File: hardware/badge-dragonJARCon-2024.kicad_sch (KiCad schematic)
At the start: 32 parts, among them J1 UART, J2 Battery, J3 OLED, J5 Shitty addon, P1 USB_C_Plug_USB2.0, Q1 DMG3415U-7, SW1 ON, SW2 RESET, SW3 BOOT, SW4 PB4, SW5 PB3, SW6 PB1, SW7 PB2, U1 ESP32-C6-WROOM-1U-N4, U2 AP2112K-3.3

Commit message: feat(Hw): Init floorplan
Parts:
- removed C9: 0.1uF, Capacitor_SMD:C_0603_1608Metric, symbol Device:C
- removed D3: WS2812B, Ekoparty:LED_SK6812MINI_PLCC4_3.5x3.5mm_P1.75mm, symbol LED:WS2812B
- removed R6: 470, Resistor_SMD:R_0603_1608Metric, symbol Device:R
- removed U1: ESP32-C6-WROOM-1U-N4, Footprint:MOD28_ESP32-C6-WROOM-1U_EXP, symbol Minino:ESP32-C6-WROOM-1U-N8
- added C10, C11: 10uF, Capacitor_SMD:C_0603_1608Metric, symbol Device:C_Small
- added C9: 1uF, Capacitor_SMD:C_0603_1608Metric, symbol Device:C_Small
- added D2: LED_RABG, Footprints:AAA3528SURKCGKC09, symbol Device:LED_RABG
- added R5, R7, R8: 330, Resistor_SMD:R_0603_1608Metric, symbol Device:R
- added U1: ESP32-C6-WROOM-1-N4, Footprints:ESP32C6WROOM1N4, symbol ESP32-C6-WROOM-1-N4:ESP32-C6-WROOM-1-N4
- J2: footprint Footprint:BAT-TH_BH-AAA-A1AJ024 -> Footprints:BAT-TH_BH-AAA-A1AJ024
- J3: footprint Connector_PinHeader_2.54mm:PinHeader_1x04_P2.54mm_Vertical -> Footprints:Display OLED 128 x32
- J5: footprint (none) -> Connector_PinHeader_2.54mm:PinHeader_2x02_P2.54mm_Vertical
- P1: footprint Footprint:C393939 -> Footprints:C393939
- SW1: footprint Footprint:JS102011SAQN -> Footprints:JS102011SAQN
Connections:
- net +3V3: now also C10.1, C11.1, C9.1, D2.2 (A), U1.2 (3V3)
- net BOOT: now also U1.15 (IO9)
- net D+: now also U1.14 (IO13)
- net D-: now also U1.13 (IO12)
- net EN: now also U1.3 (EN)
- net GND: now also C10.2, C11.2, C9.2, U1.1 (GND_1), U1.28 (GND_2), U1.29 (GND_3), U1.30 (GND_4), U1.31 (GND_5), U1.32 (GND_6), U1.33 (GND_7), U1.34 (GND_8), U1.35 (GND_9), U1.36 (GND_10), U1.37 (GND_11)
- net RX: now also U1.24 (RXD0)
- net SCL: now also U1.7 (IO7)
- net SDA: now also U1.6 (IO6)
- net TX: now also U1.25 (TXD0)
- new net: D2.1 (RK), R5.2
- new net: D2.3 (BK), R8.2
- new net: D2.4 (GK), R7.2
- new net BACK: U1.20 (IO22)
- new net BLUE: R8.1, U1.12 (IO11)
- new net DOWN: U1.21 (IO23)
- new net GREEN: R7.1, U1.26 (IO3)
- new net RED: R5.1, U1.27 (IO2)
- new net SELECT: U1.9 (IO1)
- new net UP: U1.23 (IO15)
- no-connect marks 13 -> 9
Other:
- note added: "MICROCONTROLLER"
- note removed: "ESP32-C6"
- moved on the sheet: F1, P1, R2, R3

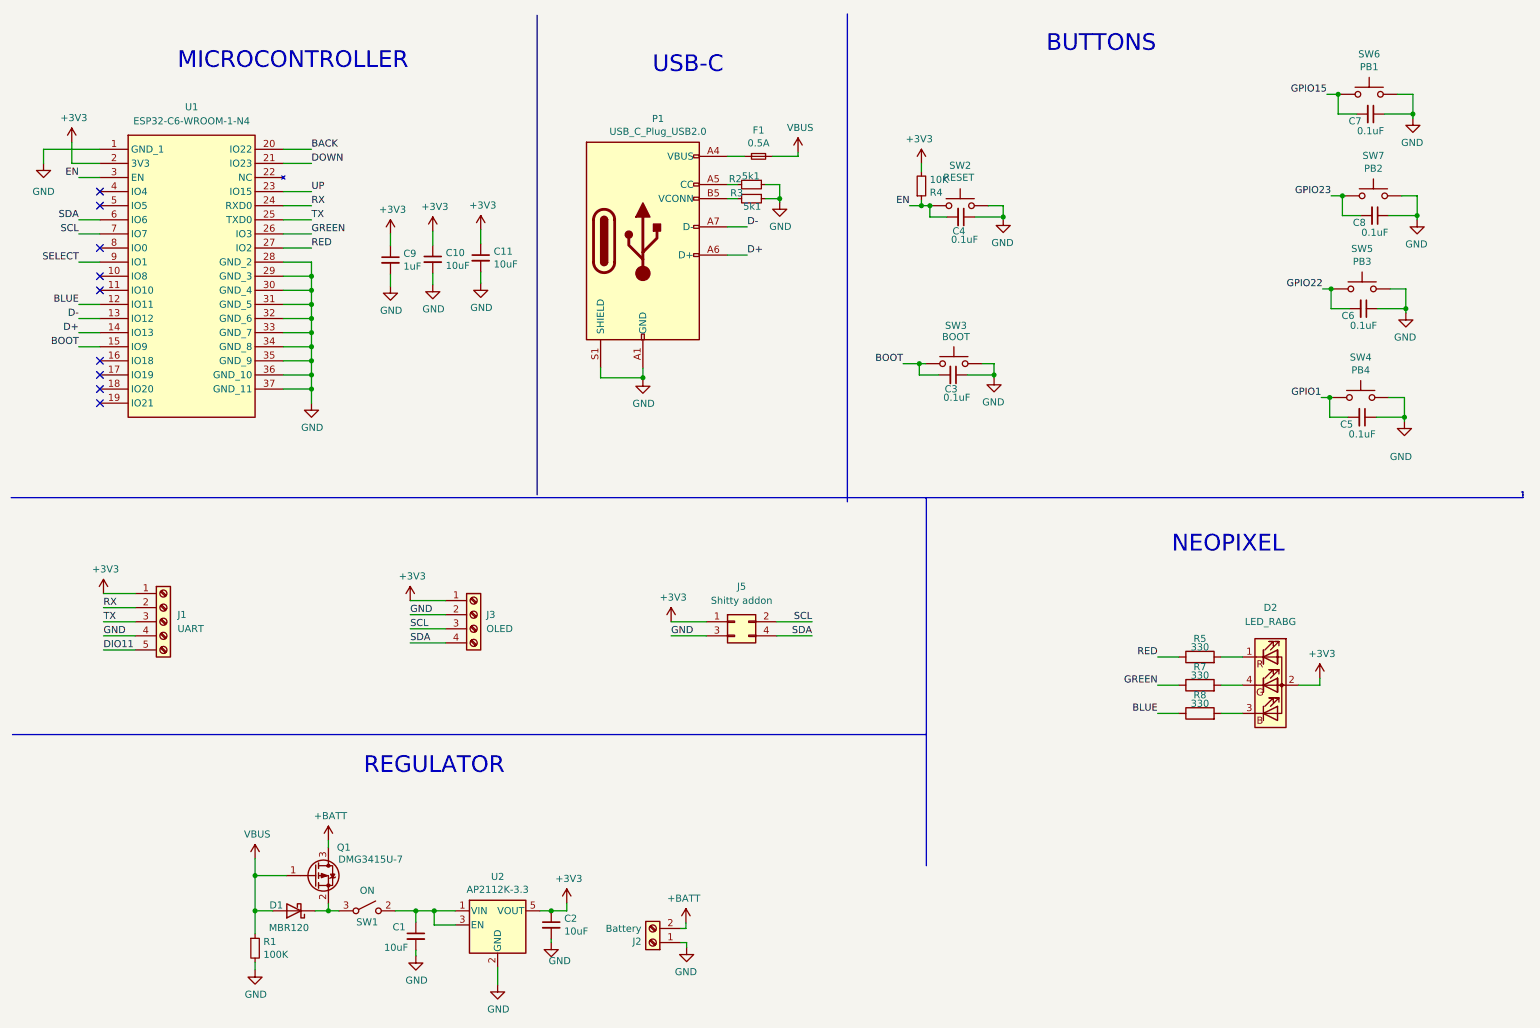
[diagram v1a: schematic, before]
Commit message: feat(Hw): Start new floorplan
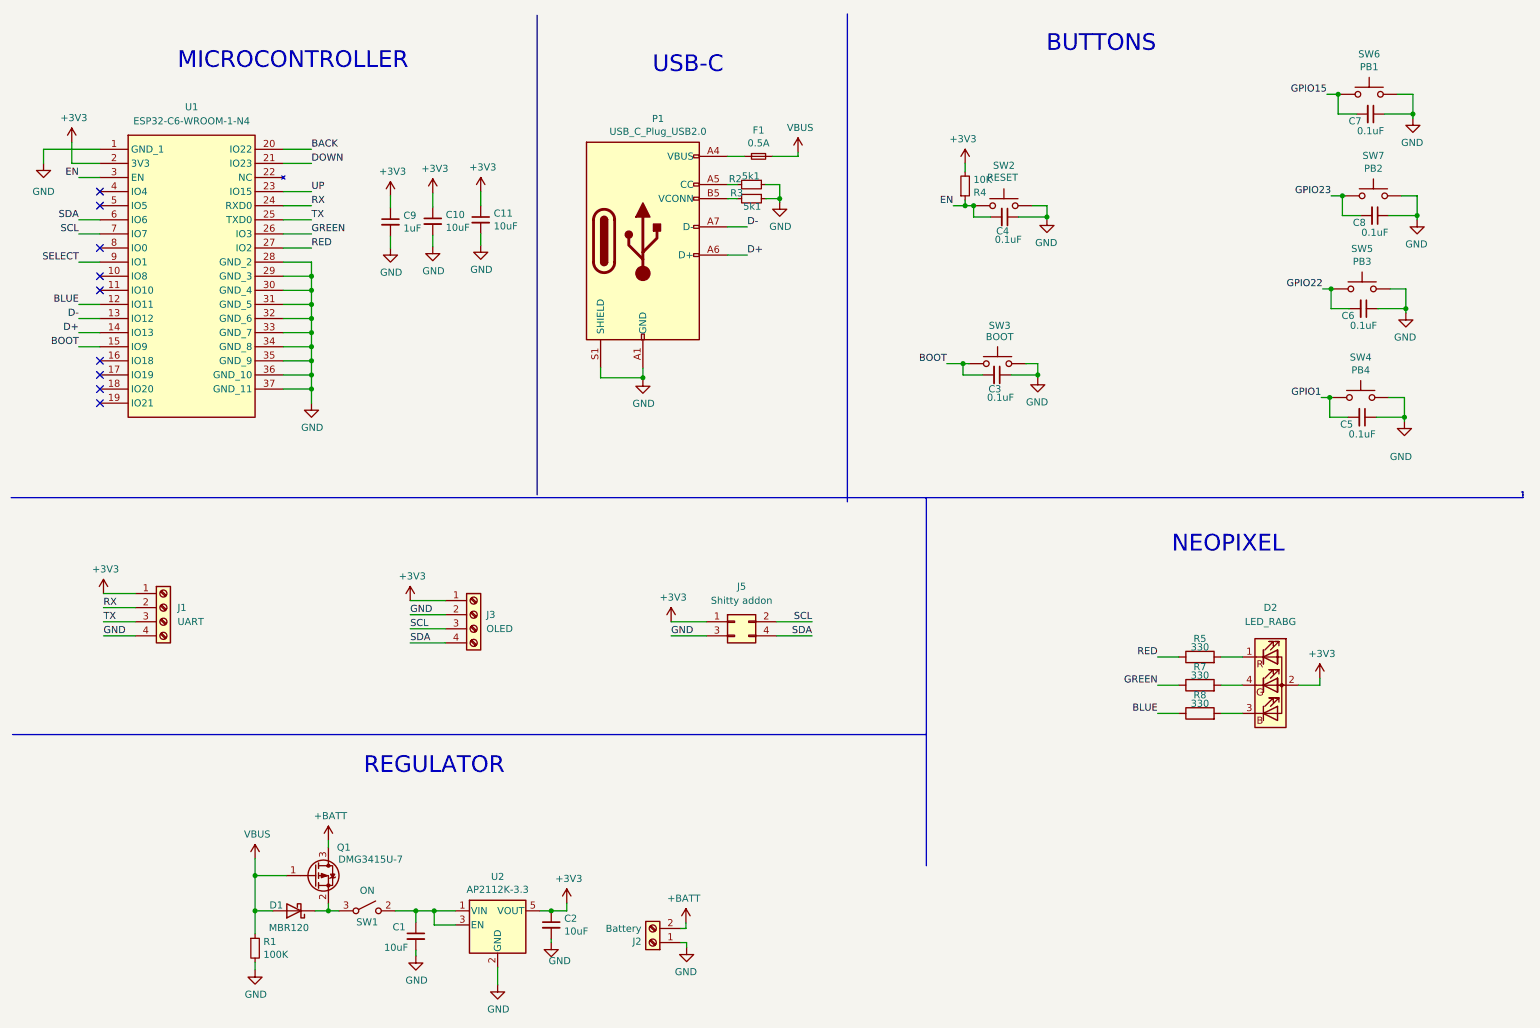
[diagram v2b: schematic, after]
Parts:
- removed J1: UART, Connector_PinHeader_2.54mm:PinHeader_1x05_P2.54mm_Vertical, symbol Connector:Screw_Terminal_01x05
- added J1: UART, Footprints:Display OLED 128 x32, symbol Connector:Screw_Terminal_01x04
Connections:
- net +3V3: now also J1.1 (Pin_1)
- net GND: now also J1.4 (Pin_4)
- net RX: now also J1.2 (Pin_2)
- net TX: now also J1.3 (Pin_3)
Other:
- moved on the sheet: C10, C11, C3, C4, C9, R4, SW2, SW3

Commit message: feat(Hw): Init routing
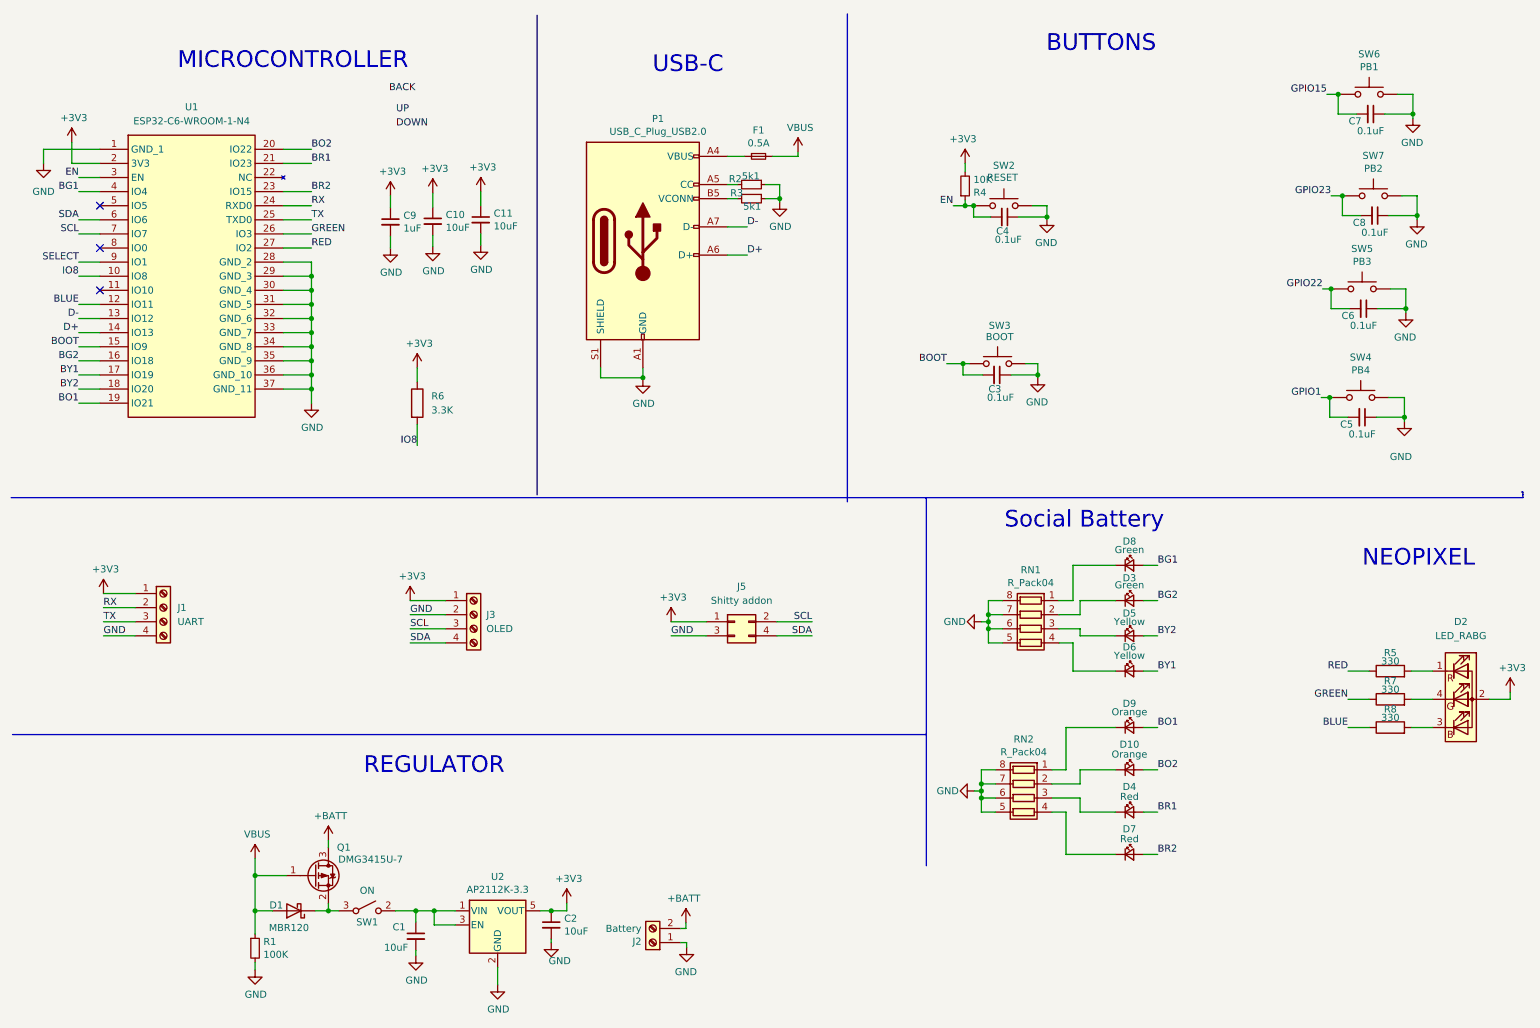
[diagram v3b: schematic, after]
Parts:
- added D10, D9: Orange, LED_SMD:LED_0805_2012Metric, symbol Device:LED_Small
- added D3, D8: Green, LED_SMD:LED_0805_2012Metric, symbol Device:LED_Small
- added D4, D7: Red, LED_SMD:LED_0805_2012Metric, symbol Device:LED_Small
- added D5, D6: Yellow, LED_SMD:LED_0805_2012Metric, symbol Device:LED_Small
- added R6: 3.3K, Resistor_SMD:R_0603_1608Metric, symbol Device:R
- added RN1, RN2: R_Pack04, Resistor_SMD:R_Array_Convex_4x0603, symbol Device:R_Pack04
- J1: footprint Footprints:Display OLED 128 x32 -> Footprints:PinHeader_1x04_P2.54mm_Vertical
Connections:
- net +3V3: now also R6.1
- net BACK: no longer U1.20 (IO22)
- net DOWN: no longer U1.21 (IO23)
- net GND: now also RN1.5 (R4.2), RN1.6 (R3.2), RN1.7 (R2.2), RN1.8 (R1.2), RN2.5 (R4.2), RN2.6 (R3.2), RN2.7 (R2.2), RN2.8 (R1.2)
- net UP: no longer U1.23 (IO15)
- net IO8: now reaches U1.10 (IO8)
- net IO8: now also R6.2
- net BG2: now reaches U1.16 (IO18)
- net BG2: now also D3.2 (A)
- net BY1: now reaches U1.17 (IO19)
- net BY1: now also D6.2 (A)
- net BY2: now reaches U1.18 (IO20)
- net BY2: now also D5.2 (A)
- net BO1: now reaches U1.19 (IO21)
- net BO1: now also D9.2 (A)
- net BG1: now reaches U1.4 (IO4)
- net BG1: now also D8.2 (A)
- new net: D9.1 (K), RN2.1 (R1.1)
- new net: D10.1 (K), RN2.2 (R2.1)
- new net: D4.1 (K), RN2.3 (R3.1)
- new net: D7.1 (K), RN2.4 (R4.1)
- new net: D8.1 (K), RN1.1 (R1.1)
- new net: D5.1 (K), RN1.3 (R3.1)
- new net: D3.1 (K), RN1.2 (R2.1)
- new net: D6.1 (K), RN1.4 (R4.1)
- new net BO2: D10.2 (A), U1.20 (IO22)
- new net BR1: D4.2 (A), U1.21 (IO23)
- new net BR2: D7.2 (A), U1.23 (IO15)
- no-connect marks 9 -> 3
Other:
- note added: "Social Battery"
- moved on the sheet: D2, R5, R7, R8

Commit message: feat(Hw): Update PCB
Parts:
- C3, C4, C5, C6, C7, C8: LCSC# C42998 -> C282670
- J1: manf# Display OLED 128×32 0.91 I2C SSD1306 Blanco / Azul -> (none); now not fitted
- J5: manf# (none) -> SSW-101-06-T-Q
- R6: LCSC# C22978 -> C118393
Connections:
- net GPIO1 is gone; now on net UP: C5.2, SW4.2
- net GPIO15 is gone; now on net BACK: C7.2, SW6.2
- net GPIO22 is gone; now on net DOWN: C6.2, SW5.2
- net GPIO23 is gone; now on net SELECT: C8.2, SW7.2
- net +3V3: now also J3.3 (Pin_3); no longer J3.1 (Pin_1)
- net BACK: now also U1.5 (IO5)
- net BLUE: now also U1.26 (IO3); no longer U1.12 (IO11)
- net DOWN: now also U1.9 (IO1)
- net GND: now also J3.4 (Pin_4); no longer J3.2 (Pin_2)
- net GREEN: now also U1.27 (IO2); no longer U1.26 (IO3)
- net RED: now also U1.12 (IO11); no longer U1.27 (IO2)
- net RX: now also J1.3 (Pin_3); no longer J1.2 (Pin_2)
- net SCL: now also J3.2 (Pin_2), J5.4 (Pin_4); no longer J3.3 (Pin_3), J5.2 (Pin_2)
- net SDA: now also J3.1 (Pin_1), J5.2 (Pin_2); no longer J3.4 (Pin_4), J5.4 (Pin_4)
- net SELECT: now also U1.11 (IO10); no longer U1.9 (IO1)
- net TX: now also J1.2 (Pin_2); no longer J1.3 (Pin_3)
- net UP: now also U1.8 (IO0)
- net at D5.1 (K): now also RN1.4 (R4.1); no longer RN1.3 (R3.1)
- net at D6.1 (K): now also RN1.3 (R3.1); no longer RN1.4 (R4.1)
- no-connect marks 3 -> 0
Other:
- moved on the sheet: C6, C8, D5, D6, SW5, SW7

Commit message: feat(Hw): Update BOM
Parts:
- F1: value 0.5A -> 0.75A; footprint Fuse:Fuse_0805_2012Metric -> Fuse:Fuse_0603_1608Metric; LCSC# C1972808 -> C182438
- SW1: footprint Footprints:JS102011SAQN -> Footprints:MSK12C02; LCSC# - -> C431540; manf# 611-JS102011SAQN -> (none)
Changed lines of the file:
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@@
 			)
 		)
-		(property "Footprint" "Footprints:JS102011SAQN"
+		(property "Footprint" "Footprints:MSK12C02"
 			(at 76.073 173.99 0)
 			(effects
@@
 			)
 		)
-		(property "LCSC#" "-"
+		(property "LCSC#" "C431540"
 			(at 76.073 173.99 0)
 			(effects
@@
 			)
 		)
-		(property "manf#" "611-JS102011SAQN"
+		(property "manf#" ""
 			(at 76.073 173.99 0)
 			(effects
@@
 			)
 		)
-		(property "Value" "0.5A"
+		(property "Value" "0.75A"
 			(at 146.558 35.7124 0)
 			(effects
@@
 			)
 		)
-		(property "Footprint" "Fuse:Fuse_0805_2012Metric"
+		(property "Footprint" "Fuse:Fuse_0603_1608Metric"
 			(at 146.558 38.1 0)
 			(effects
@@
 			)
 		)
-		(property "LCSC#" "C1972808"
+		(property "LCSC#" " C182438"
 			(at 146.558 38.1 0)
 			(effects

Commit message: feat(Hw): Revisado
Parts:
- U2: LCSC# C150742 -> C51118
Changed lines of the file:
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@@
 			)
 		)
-		(property "LCSC#" "C150742"
+		(property "LCSC#" "C51118"
 			(at 99.568 176.53 0)
 			(effects
